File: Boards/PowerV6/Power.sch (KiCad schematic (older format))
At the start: 111 parts, among them IC1 PIC32MM0064GPM048, K1 Relay(Mech/SSR), K2 Relay(Mech/SSR), K3 Relay(Mech/SSR), K4 Relay(Mech/SSR), K5 Relay(Mech/SSR), K6 Relay(Mech/SSR), K7 Relay(Mech/SSR), K8 Relay(Mech/SSR), P1 L1, P10 1x6 2.54 Pin Header, P11 Stacked USBA, P12 Mains, P13 Mains, P2 L1, P3 L1, P4 L1, P5 L1, P6 L1, P7 L1, P8 L1, P9 1x2 2.54, Q1 NX7002AK, Q10 NX7002AK, Q11 NX7002AK, Q12 AO3407A, Q2 NX7002AK, Q3 NX7002AK, Q4 NX7002AK, Q5 NX7002AK, Q6 NX7002AK, Q7 NX7002AK, Q8 NX7002AK, Q9 NX7002AK, U1 ST485EC, U2 AP2114H, U3 LTV-826, U4 LTV-826, X1 8MHz

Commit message: working on power refactor
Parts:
- removed C?: 100nF, Capacitors_SMD:C_0805, symbol C_Small
- removed D?: SMBJ30D, Diodes_SMD:D_SMB, symbol D_TVS_ALT
- removed D?: BZX84C3V3, Diodes_SMD:D_SOT-23_ANK, symbol D_Zener_ALT
- removed R?: 100R, Resistors_SMD:R_0805, symbol R
- D1, D11, D13, D15, D19, D3, D5, D7, D9: footprint LEDs:LED-0805 -> LEDs:LED_0805
- D10, D12, D14, D16, D2, D4, D6, D8: footprint Diodes_SMD:Diode-SMA_Standard -> Diodes_SMD:D_SMA
- IC1: footprint (none) -> Housings_DFN_QFN:QFN-48-1EP_6x6mm_Pitch0.4mm
- K1, K2, K3, K4, K5, K6, K7, K8: footprint A_MyFootPrints:Relay-Mech-SSR -> MyFootPrints:Relay-Mech-SSR
- P1, P2, P3, P4, P5, P6, P7, P8: value L1 -> Stab and 1x3; footprint A_MyFootPrints:Screw_Header_1x1_5.08 -> MyFootPrints:Current_Board
- P12, P13: footprint A_MyFootPrints:Screw_Header_1x1_5.08 -> MyFootPrints:Screw_Header_1x2_5.08; symbol CONN_01X01 -> Conn_01x02
- P9: footprint MyFootPrints:Screw_Header_1x4 -> MyFootPrints:Screw_Header_1x2
- Q1, Q2, Q3, Q4, Q5, Q6, Q7, Q8: footprint Housings_SOT-23_SOT-143_TSOT-6:SOT-23 -> TO_SOT_Packages_SMD:SOT-23
- U3, U4: footprint A_MyFootPrints:8_SMD_GULL_WING -> MyFootPrints:8_SMD_GULL_WING
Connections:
- net +5V: now also P2.2 (Pin_2), P3.2 (Pin_2), P4.2 (Pin_2), P5.2 (Pin_2), P6.2 (Pin_2), P7.2 (Pin_2), P8.2 (Pin_2)
- net CURRENT_1: now also P1.3 (Pin_3)
- net CURRENT_2: now also P2.3 (Pin_3)
- net CURRENT_3: now also P3.3 (Pin_3)
- net CURRENT_4: now also P4.3 (Pin_3)
- net CURRENT_5: now also P5.3 (Pin_3)
- net CURRENT_6: now also P6.3 (Pin_3)
- net CURRENT_7: now also P7.3 (Pin_3)
- net CURRENT_8: now also P8.3 (Pin_3)
- net GND: now also P2.4 (Pin_4), P3.4 (Pin_4), P4.4 (Pin_4), P5.4 (Pin_4), P6.4 (Pin_4), P7.4 (Pin_4), P8.4 (Pin_4)
- net N: now also P12.2 (Pin_2), P13.2 (Pin_2)
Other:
- note added: "Relay for Plug 1"
- note added: "Relay for Plug 2"
- note added: "Relay for Plug 3"
- note added: "Relay for Plug 4"
- note added: "Relay for Plug 5"
- note added: "Relay for Plug 6"
- note added: "Relay for Plug 7"
- note added: "Relay for Plug 8"
- moved on the sheet: C1, C2, C3, C4, C5, C6, C7, D1, D10, D11, D12, D13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

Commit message: working on power pcb
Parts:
- removed P9: 1x2 2.54, MyFootPrints:Screw_Header_1x2, symbol Conn_01x02
- removed Q12: AO3407A, TO_SOT_Packages_SMD:SOT-23, symbol MOSFET_P_SMALL
- IC1: footprint Housings_DFN_QFN:QFN-48-1EP_6x6mm_Pitch0.4mm -> Housings_QFP:TQFP-48_7x7mm_Pitch0.5mm
- P12, P13: value Mains -> 1x2 5.08
- R38: value 300R -> 150R
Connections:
- net AC_AVAIL: now also D19.1 (K); no longer D19.2 (A)
- net CURRENT_1: now also IC1.25 (RB2); no longer IC1.21 (RA0)
- net CURRENT_2: now also IC1.24 (RB1); no longer IC1.22 (RA1)
- net CURRENT_3: now also IC1.26 (RB3); no longer IC1.23 (RB0)
- net CURRENT_4: now also IC1.23 (RB0); no longer IC1.24 (RB1)
- net CURRENT_5: now also IC1.27 (RC0); no longer IC1.25 (RB2)
- net CURRENT_6: now also IC1.22 (RA1); no longer IC1.26 (RB3)
- net CURRENT_7: now also IC1.28 (RC1); no longer IC1.27 (RC0)
- net CURRENT_8: now also IC1.21 (RA0); no longer IC1.28 (RC1)
- net RELAY_1: now also IC1.35 (RB4); no longer IC1.16 (RB15)
- net RELAY_2: now also IC1.14 (RA7); no longer IC1.15 (RB14)
- net RELAY_3: now also IC1.36 (RA4); no longer IC1.14 (RA7)
- net RELAY_5: now also IC1.46 (RB6); no longer IC1.12 (RB13)
- net RELAY_6: now also IC1.4 (RC8); no longer IC1.10 (RB11)
- net RELAY_7: now also IC1.47 (RB7); no longer IC1.9 (RB10)
- net RELAY_8: now also IC1.1 (RB9); no longer IC1.8 (RA15)
- net at R38.1: now also D19.2 (A); no longer D19.1 (K)
- no-connect marks 10 -> 5
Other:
- note removed: "Power Input and \nReverse Cicuit Protection"
- moved on the sheet: D19

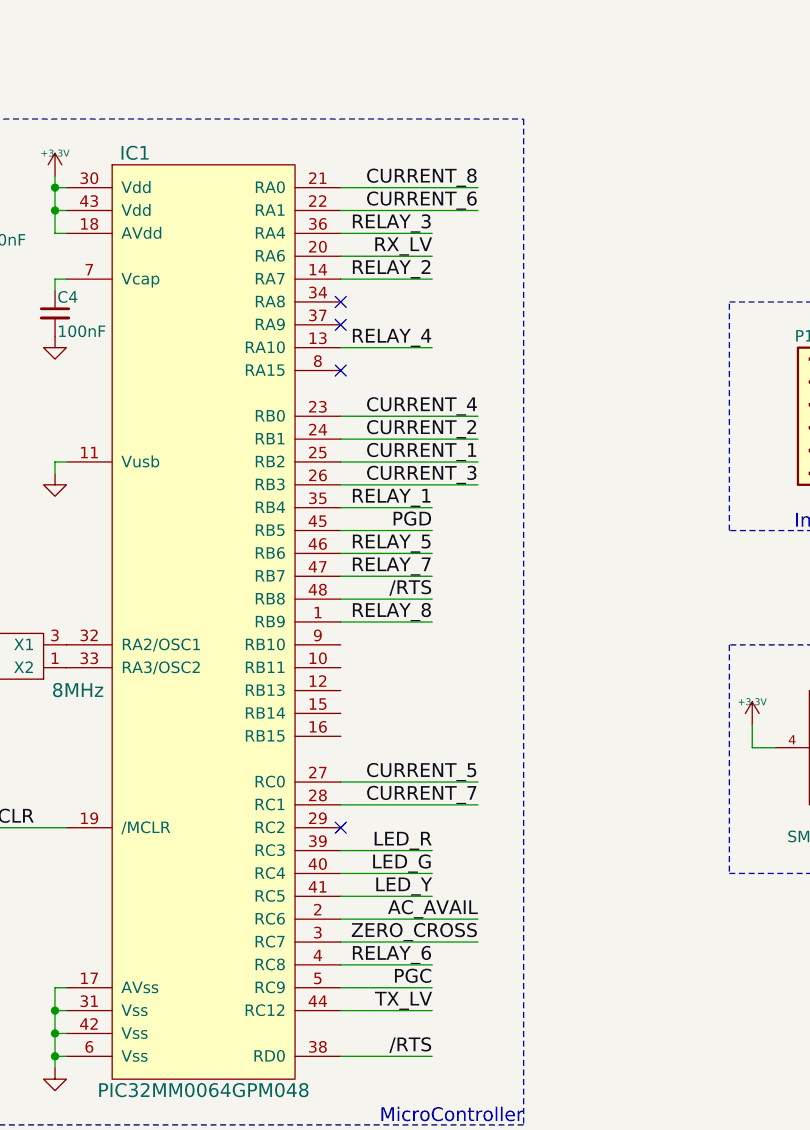
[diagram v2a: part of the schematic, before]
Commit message: finished power board layout and fixed pin mappings
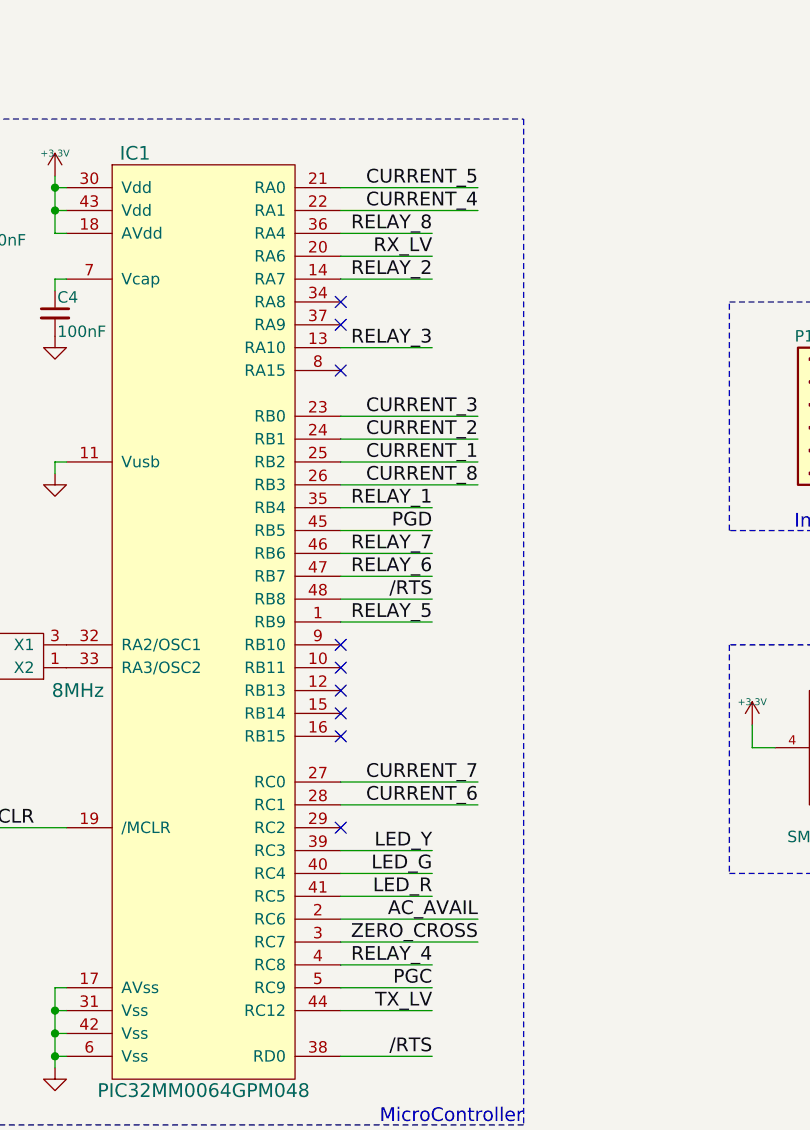
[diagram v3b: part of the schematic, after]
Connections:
- net CURRENT_3: now also IC1.23 (RB0); no longer IC1.26 (RB3)
- net CURRENT_4: now also IC1.22 (RA1); no longer IC1.23 (RB0)
- net CURRENT_5: now also IC1.21 (RA0); no longer IC1.27 (RC0)
- net CURRENT_6: now also IC1.28 (RC1); no longer IC1.22 (RA1)
- net CURRENT_7: now also IC1.27 (RC0); no longer IC1.28 (RC1)
- net CURRENT_8: now also IC1.26 (RB3); no longer IC1.21 (RA0)
- net LED_R: now also IC1.41 (RC5); no longer IC1.39 (RC3)
- net LED_Y: now also IC1.39 (RC3); no longer IC1.41 (RC5)
- net RELAY_3: now also IC1.13 (RA10); no longer IC1.36 (RA4)
- net RELAY_4: now also IC1.4 (RC8); no longer IC1.13 (RA10)
- net RELAY_5: now also IC1.1 (RB9); no longer IC1.46 (RB6)
- net RELAY_6: now also IC1.47 (RB7); no longer IC1.4 (RC8)
- net RELAY_7: now also IC1.46 (RB6); no longer IC1.47 (RB7)
- net RELAY_8: now also IC1.36 (RA4); no longer IC1.1 (RB9)
- no-connect marks 5 -> 10
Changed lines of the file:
@@
 RX_LV
 Text Label 4200 9300 2    60   ~ 0
-LED_R
+LED_Y
 Text Label 4200 9400 2    60   ~ 0
 LED_G
 Text Label 4200 9500 2    60   ~ 0
-LED_Y
+LED_R
 $Comp
 L TRI-LED D17
@@
 AC_AVAIL
 Text Label 4200 7100 2    60   ~ 0
-RELAY_4
+RELAY_3
 Text Label 4200 7800 2    60   ~ 0
 RELAY_1
 Text Label 4200 6600 2    60   ~ 0
-RELAY_3
+RELAY_8
 Text Label 4200 6800 2    60   ~ 0
 RELAY_2
 Text Label 4200 8000 2    60   ~ 0
+RELAY_7
+Text Label 4200 8300 2    60   ~ 0
 RELAY_5
-Text Label 4200 8300 2    60   ~ 0
-RELAY_8
 Text Label 4200 8100 2    60   ~ 0
-RELAY_7
+RELAY_6
 Text Label 4200 9800 2    60   ~ 0
-RELAY_6
+RELAY_4
 Text Label 4400 7500 2    60   ~ 0
 CURRENT_2
@@
 	3800 7700 4400 7700
 Text Label 4400 7700 2    60   ~ 0
+CURRENT_8
+Text Label 4400 7400 2    60   ~ 0
 CURRENT_3
-Text Label 4400 7400 2    60   ~ 0
+Text Label 4400 9000 2    60   ~ 0
+CURRENT_7
+Text Label 4400 6500 2    60   ~ 0
 CURRENT_4
-Text Label 4400 9000 2    60   ~ 0
+Text Label 4400 9100 2    60   ~ 0
+CURRENT_6
+Text Label 4400 6400 2    60   ~ 0
 CURRENT_5
-Text Label 4400 6500 2    60   ~ 0
-CURRENT_6
-Text Label 4400 9100 2    60   ~ 0
-CURRENT_7
-Text Label 4400 6400 2    60   ~ 0
-CURRENT_8
 NoConn ~ 3800 6900
 NoConn ~ 3800 7000
@@
 Wire Wire Line
 	4200 7800 3800 7800
+NoConn ~ 3800 8400
+NoConn ~ 3800 8500
+NoConn ~ 3800 8600
+NoConn ~ 3800 8700
+NoConn ~ 3800 8800
 $EndSCHEMATC

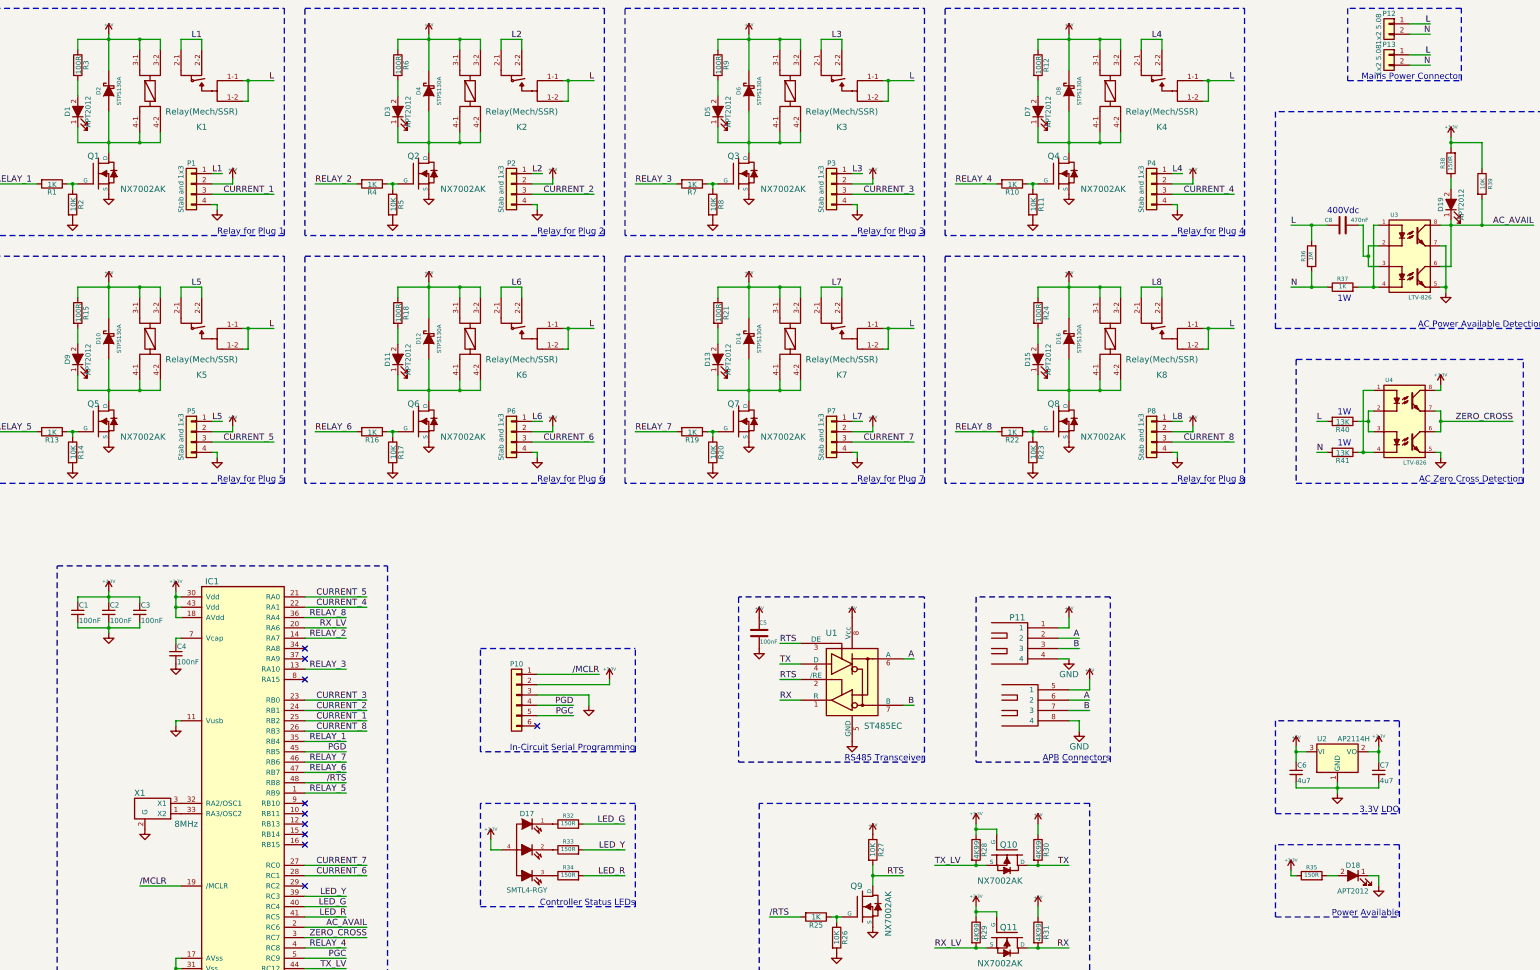
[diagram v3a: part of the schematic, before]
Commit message: added power bom
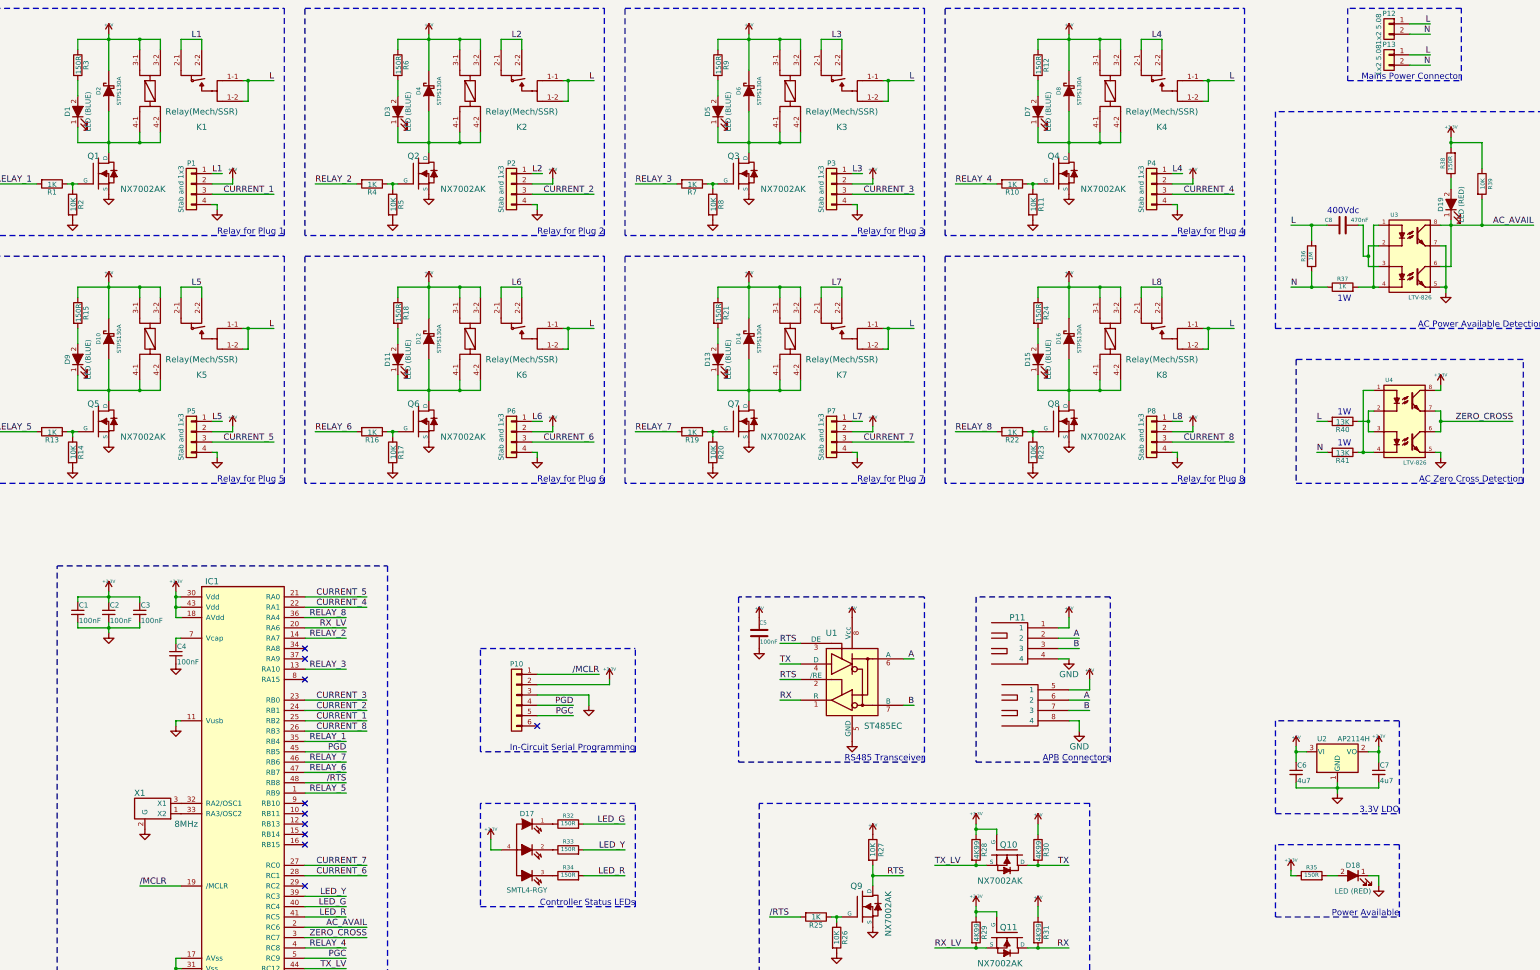
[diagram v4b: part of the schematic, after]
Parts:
- D1, D11, D13, D15, D3, D5, D7, D9: value APT2012 -> LED (BLUE)
- D18, D19: value APT2012 -> LED (RED)
- IC1: Manufacter Part Number (none) -> PIC32MM0064GPM048T-I/PT
- R12, R15, R18, R21, R24, R3, R6, R9: value 100R -> 150R
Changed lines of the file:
@@
 P 14900 2600
 F 0 "D19" H 14900 2700 50  0000 C CNN
-F 1 "APT2012" H 14900 2500 50  0000 C CNN
+F 1 "LED (RED)" H 14900 2500 50  0000 C CNN
 F 2 "LEDs:LED_0805" H 14900 2600 60  0001 C CNN
 F 3 "~" H 14900 2600 60  0000 C CNN
@@
 P 1600 1250
 F 0 "R3" V 1680 1250 50  0000 C CNN
-F 1 "100R" V 1607 1251 50  0000 C CNN
+F 1 "150R" V 1607 1251 50  0000 C CNN
 F 2 "Resistors_SMD:R_0805" V 1530 1250 30  0001 C CNN
 F 3 "" H 1600 1250 30  0000 C CNN
@@
 P 1600 1700
 F 0 "D1" H 1600 1800 50  0000 C CNN
-F 1 "APT2012" H 1600 1600 50  0000 C CNN
+F 1 "LED (BLUE)" H 1600 1600 50  0000 C CNN
 F 2 "LEDs:LED_0805" H 1600 1700 60  0001 C CNN
 F 3 "~" H 1600 1700 60  0000 C CNN
@@
 P 13950 9100
 F 0 "D18" H 13950 9200 50  0000 C CNN
-F 1 "APT2012" H 13950 8950 50  0000 C CNN
+F 1 "LED (RED)" H 13950 8950 50  0000 C CNN
 F 2 "LEDs:LED_0805" H 13950 9100 60  0001 C CNN
 F 3 "~" H 13950 9100 60  0000 C CNN
@@
 F 2 "Housings_QFP:TQFP-48_7x7mm_Pitch0.5mm" H 3500 8050 60  0001 C CNN
 F 3 "" H 3500 8050 60  0001 C CNN
+F 4 " PIC32MM0064GPM048T-I/PT " H 3200 8300 60  0001 C CNN "Manufacter Part Number"
 	1    3200 8300
 	1    0    0    -1
@@
 P 4700 1250
 F 0 "R6" V 4780 1250 50  0000 C CNN
-F 1 "100R" V 4707 1251 50  0000 C CNN
+F 1 "150R" V 4707 1251 50  0000 C CNN
 F 2 "Resistors_SMD:R_0805" V 4630 1250 30  0001 C CNN
 F 3 "" H 4700 1250 30  0000 C CNN
@@
 P 4700 1700
 F 0 "D3" H 4700 1800 50  0000 C CNN
-F 1 "APT2012" H 4700 1600 50  0000 C CNN
+F 1 "LED (BLUE)" H 4700 1600 50  0000 C CNN
 F 2 "LEDs:LED_0805" H 4700 1700 60  0001 C CNN
 F 3 "~" H 4700 1700 60  0000 C CNN
@@
 P 7800 1250
 F 0 "R9" V 7880 1250 50  0000 C CNN
-F 1 "100R" V 7807 1251 50  0000 C CNN
+F 1 "150R" V 7807 1251 50  0000 C CNN
 F 2 "Resistors_SMD:R_0805" V 7730 1250 30  0001 C CNN
 F 3 "" H 7800 1250 30  0000 C CNN
@@
 P 7800 1700
 F 0 "D5" H 7800 1800 50  0000 C CNN
-F 1 "APT2012" H 7800 1600 50  0000 C CNN
+F 1 "LED (BLUE)" H 7800 1600 50  0000 C CNN
 F 2 "LEDs:LED_0805" H 7800 1700 60  0001 C CNN
 F 3 "~" H 7800 1700 60  0000 C CNN
@@
 P 10900 1250
 F 0 "R12" V 10980 1250 50  0000 C CNN
-F 1 "100R" V 10907 1251 50  0000 C CNN
+F 1 "150R" V 10907 1251 50  0000 C CNN
 F 2 "Resistors_SMD:R_0805" V 10830 1250 30  0001 C CNN
 F 3 "" H 10900 1250 30  0000 C CNN
@@
 P 10900 1700
 F 0 "D7" H 10900 1800 50  0000 C CNN
-F 1 "APT2012" H 10900 1600 50  0000 C CNN
+F 1 "LED (BLUE)" H 10900 1600 50  0000 C CNN
 F 2 "LEDs:LED_0805" H 10900 1700 60  0001 C CNN
 F 3 "~" H 10900 1700 60  0000 C CNN
@@
 P 1600 3650
 F 0 "R15" V 1680 3650 50  0000 C CNN
-F 1 "100R" V 1607 3651 50  0000 C CNN
+F 1 "150R" V 1607 3651 50  0000 C CNN
 F 2 "Resistors_SMD:R_0805" V 1530 3650 30  0001 C CNN
 F 3 "" H 1600 3650 30  0000 C CNN
@@
 P 1600 4100
 F 0 "D9" H 1600 4200 50  0000 C CNN
-F 1 "APT2012" H 1600 4000 50  0000 C CNN
+F 1 "LED (BLUE)" H 1600 4000 50  0000 C CNN
 F 2 "LEDs:LED_0805" H 1600 4100 60  0001 C CNN
 F 3 "~" H 1600 4100 60  0000 C CNN
@@
 P 4700 3650
 F 0 "R18" V 4780 3650 50  0000 C CNN
-F 1 "100R" V 4707 3651 50  0000 C CNN
+F 1 "150R" V 4707 3651 50  0000 C CNN
 F 2 "Resistors_SMD:R_0805" V 4630 3650 30  0001 C CNN
 F 3 "" H 4700 3650 30  0000 C CNN
@@
 P 4700 4100
 F 0 "D11" H 4700 4200 50  0000 C CNN
-F 1 "APT2012" H 4700 4000 50  0000 C CNN
+F 1 "LED (BLUE)" H 4700 4000 50  0000 C CNN
 F 2 "LEDs:LED_0805" H 4700 4100 60  0001 C CNN
 F 3 "~" H 4700 4100 60  0000 C CNN
@@
 P 7800 3650
 F 0 "R21" V 7880 3650 50  0000 C CNN
-F 1 "100R" V 7807 3651 50  0000 C CNN
+F 1 "150R" V 7807 3651 50  0000 C CNN
 F 2 "Resistors_SMD:R_0805" V 7730 3650 30  0001 C CNN
 F 3 "" H 7800 3650 30  0000 C CNN
@@
 P 7800 4100
 F 0 "D13" H 7800 4200 50  0000 C CNN
-F 1 "APT2012" H 7800 4000 50  0000 C CNN
+F 1 "LED (BLUE)" H 7800 4000 50  0000 C CNN
 F 2 "LEDs:LED_0805" H 7800 4100 60  0001 C CNN
 F 3 "~" H 7800 4100 60  0000 C CNN
@@
 P 10900 3650
 F 0 "R24" V 10980 3650 50  0000 C CNN
-F 1 "100R" V 10907 3651 50  0000 C CNN
+F 1 "150R" V 10907 3651 50  0000 C CNN
 F 2 "Resistors_SMD:R_0805" V 10830 3650 30  0001 C CNN
 F 3 "" H 10900 3650 30  0000 C CNN
@@
 P 10900 4100
 F 0 "D15" H 10900 4200 50  0000 C CNN
-F 1 "APT2012" H 10900 4000 50  0000 C CNN
+F 1 "LED (BLUE)" H 10900 4000 50  0000 C CNN
 F 2 "LEDs:LED_0805" H 10900 4100 60  0001 C CNN
 F 3 "~" H 10900 4100 60  0000 C CNN
